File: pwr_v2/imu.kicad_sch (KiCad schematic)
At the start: 5 parts, among them U4 LSM6DSLTR

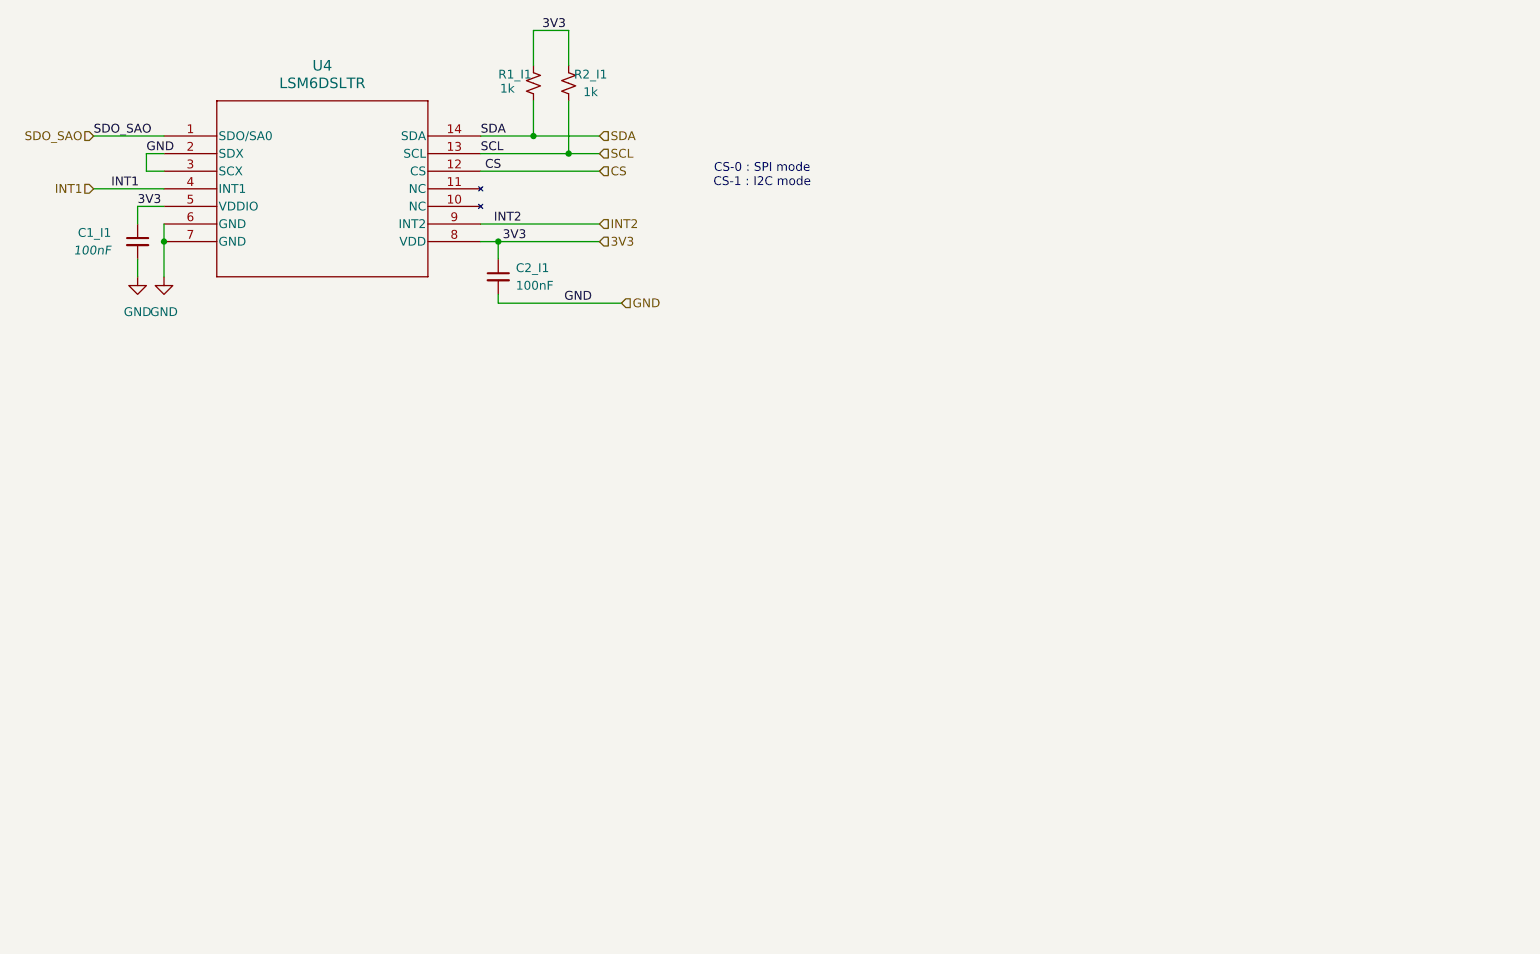
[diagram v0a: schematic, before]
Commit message: File structure enhanced.
Added uniform titleblocks and 3D renders for easier view, file cleanups.
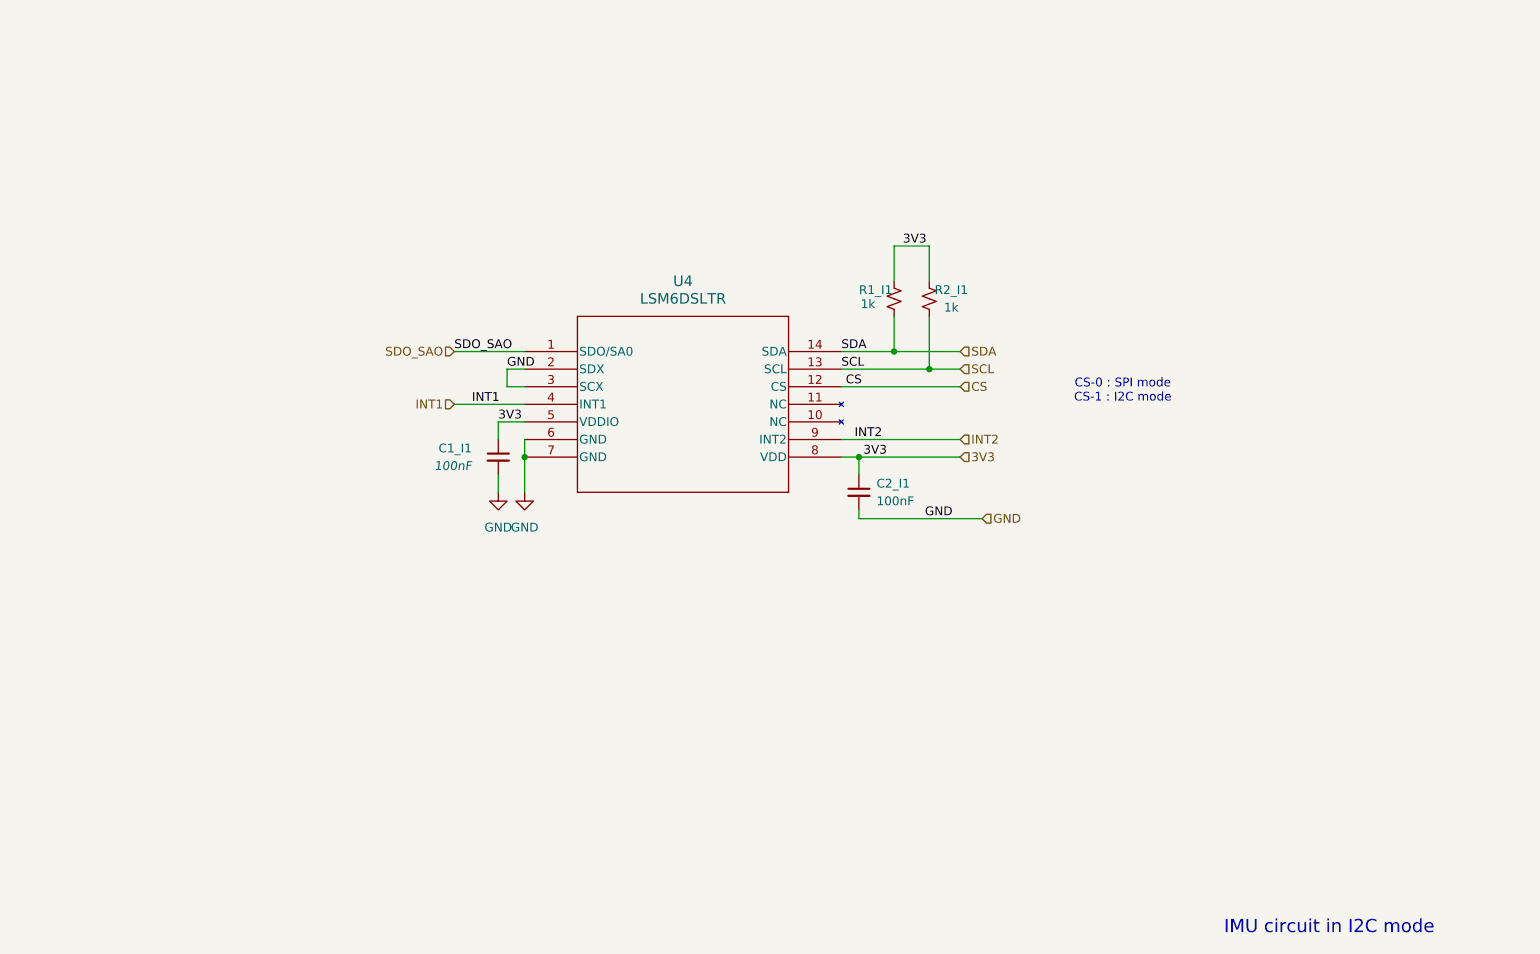
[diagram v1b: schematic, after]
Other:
- note added: "IMU circuit in I2C mode"
- company: (none) -> Buck regulator circuits to generate 12V, 5V and 3.3V supplies.
- moved on the sheet: C1_I1, C2_I1, R1_I1, R2_I1, U4
